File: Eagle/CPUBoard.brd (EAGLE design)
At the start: 100 x 80 mm, 33 parts, among them IC2 MAX232, IC3 MAX485CPA, J1 DISPLAY, J2 BUTTON_BOARD, J3 RELAY_BOARD, Q1 12.000MHz, X6 MKDSN1,5/3-5,08, X7 MKDSN1,5/3-5,08

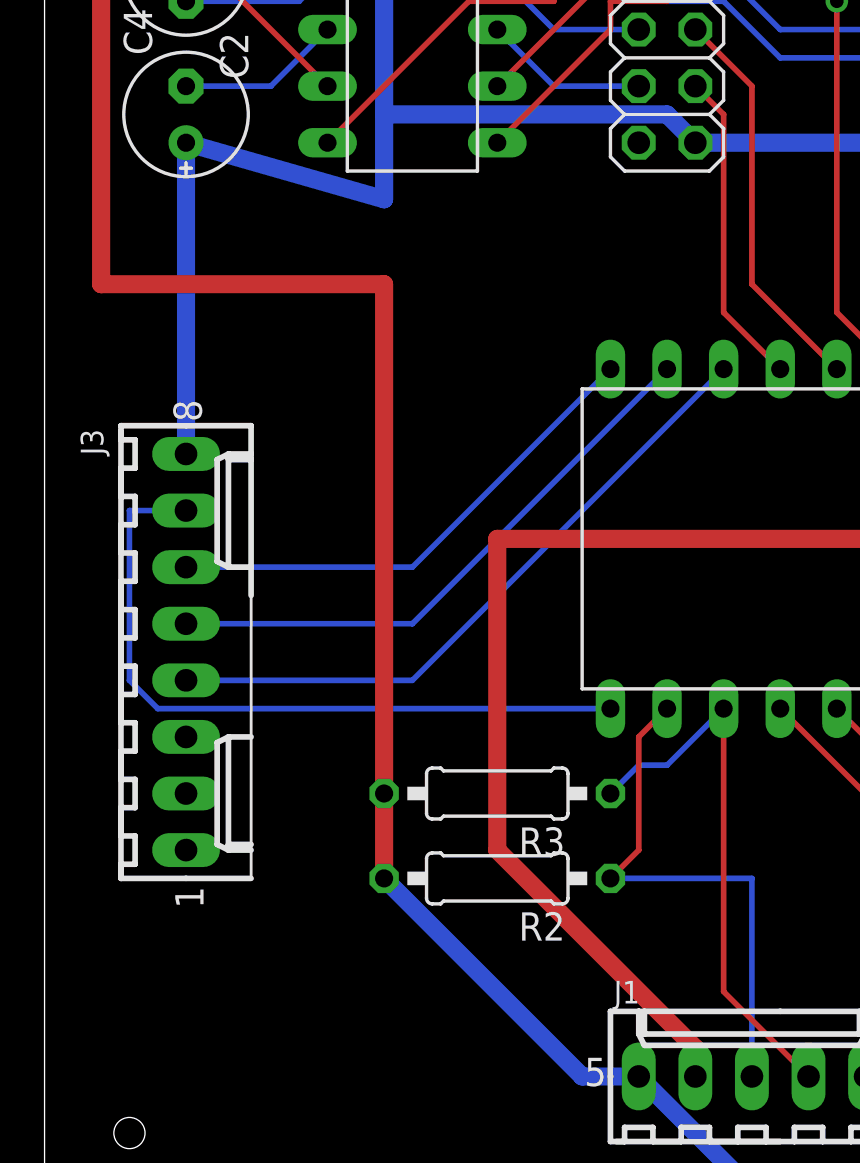
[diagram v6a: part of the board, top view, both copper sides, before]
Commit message: - swapped connections to relay board1
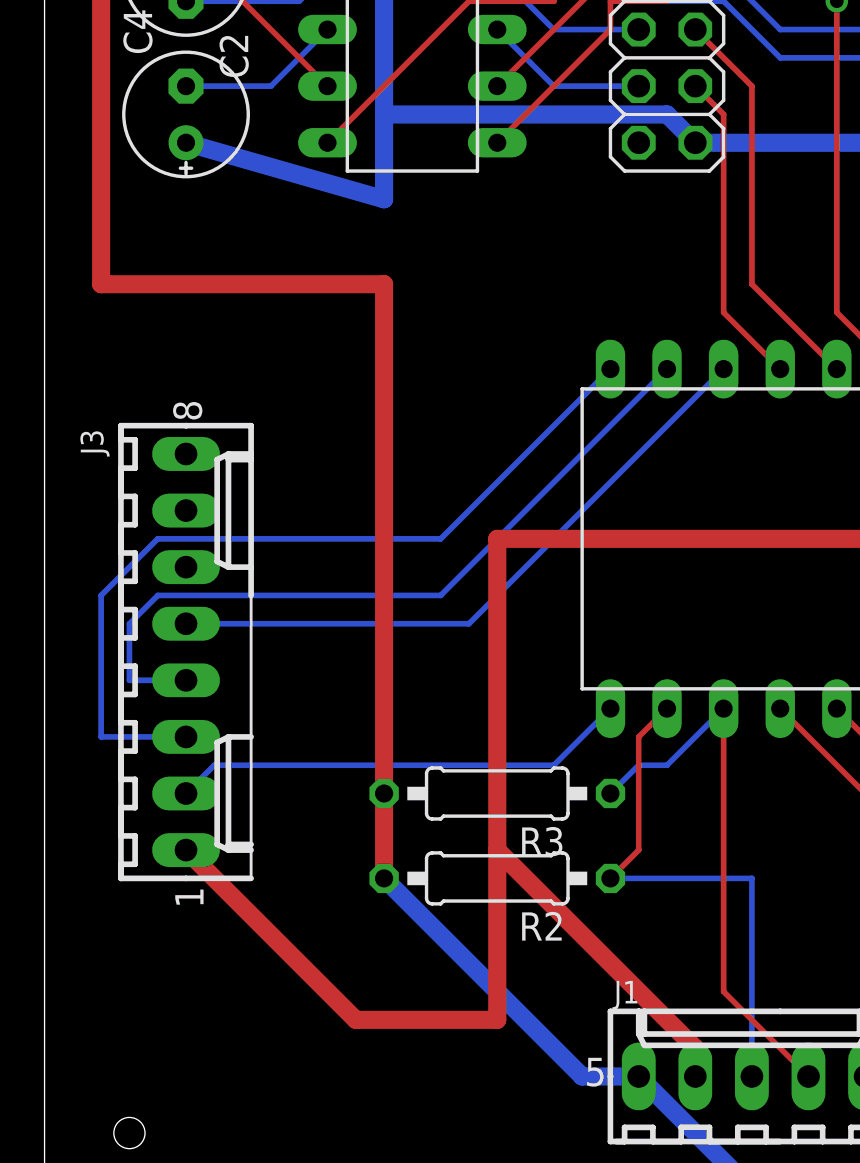
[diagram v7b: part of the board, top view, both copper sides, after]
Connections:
- net GND: now also J3.1; no longer J3.8
- net REL1: now also J3.2; no longer J3.7
- net REL2: now also J3.3; no longer J3.6
- net REL3: now also J3.4; no longer J3.5
- net REL4: now also J3.5; no longer J3.4
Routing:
- net REL2: track 22.7 -> 37.2 mm
- net REL1: track 32.3 -> 20.6 mm
- net GND: track 400.4 -> 411.2 mm
- net REL3: track 26.3 -> 33.9 mm
- net REL4: track 29.9 -> 28.9 mm
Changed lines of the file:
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@@
 <contactref element="J2" pad="10"/>
 <contactref element="JP1" pad="10"/>
-<contactref element="J3" pad="8"/>
-<wire x1="6.35" y1="34.29" x2="6.35" y2="48.26" width="0.8128" layer="16"/>
 <wire x1="45.72" y1="10.16" x2="49.53" y2="6.35" width="0.8128" layer="1"/>
 <wire x1="45.72" y1="17.78" x2="45.72" y2="10.16" width="0.8128" layer="1"/>
@@
 <wire x1="48.26" y1="44.45" x2="48.26" y2="38.1" width="0.8128" layer="16"/>
 <wire x1="43.18" y1="49.53" x2="48.26" y2="44.45" width="0.8128" layer="16"/>
+<contactref element="J3" pad="1"/>
+<wire x1="13.97" y1="8.89" x2="6.35" y2="16.51" width="0.8128" layer="1"/>
+<wire x1="20.32" y1="8.89" x2="13.97" y2="8.89" width="0.8128" layer="1"/>
+<wire x1="20.32" y1="16.51" x2="20.32" y2="8.89" width="0.8128" layer="1"/>
 </signal>
 <signal name="N$1">
@@
 <signal name="REL1">
 <contactref element="IC1" pad="21"/>
-<contactref element="J3" pad="7"/>
-<wire x1="5.08" y1="22.86" x2="25.4" y2="22.86" width="0.254" layer="16"/>
-<wire x1="3.81" y1="24.13" x2="5.08" y2="22.86" width="0.254" layer="16"/>
-<wire x1="3.81" y1="31.75" x2="3.81" y2="24.13" width="0.254" layer="16"/>
-<wire x1="6.35" y1="31.75" x2="3.81" y2="31.75" width="0.254" layer="16"/>
+<contactref element="J3" pad="2"/>
+<wire x1="22.86" y1="20.32" x2="25.4" y2="22.86" width="0.254" layer="16"/>
+<wire x1="7.62" y1="20.32" x2="22.86" y2="20.32" width="0.254" layer="16"/>
+<wire x1="6.35" y1="19.05" x2="7.62" y2="20.32" width="0.254" layer="16"/>
 </signal>
 <signal name="REL2">
 <contactref element="IC1" pad="20"/>
-<contactref element="J3" pad="6"/>
-<wire x1="16.51" y1="29.21" x2="25.4" y2="38.1" width="0.254" layer="16"/>
-<wire x1="6.35" y1="29.21" x2="16.51" y2="29.21" width="0.254" layer="16"/>
+<contactref element="J3" pad="3"/>
+<wire x1="17.78" y1="30.48" x2="25.4" y2="38.1" width="0.254" layer="16"/>
+<wire x1="5.08" y1="30.48" x2="17.78" y2="30.48" width="0.254" layer="16"/>
+<wire x1="2.54" y1="27.94" x2="5.08" y2="30.48" width="0.254" layer="16"/>
+<wire x1="2.54" y1="21.59" x2="2.54" y2="27.94" width="0.254" layer="16"/>
+<wire x1="6.35" y1="21.59" x2="2.54" y2="21.59" width="0.254" layer="16"/>
 </signal>
 <signal name="REL3">
 <contactref element="IC1" pad="19"/>
-<contactref element="J3" pad="5"/>
-<wire x1="16.51" y1="26.67" x2="27.94" y2="38.1" width="0.254" layer="16"/>
-<wire x1="6.35" y1="26.67" x2="16.51" y2="26.67" width="0.254" layer="16"/>
+<contactref element="J3" pad="4"/>
+<wire x1="17.78" y1="27.94" x2="27.94" y2="38.1" width="0.254" layer="16"/>
+<wire x1="5.08" y1="27.94" x2="17.78" y2="27.94" width="0.254" layer="16"/>
+<wire x1="3.81" y1="26.67" x2="5.08" y2="27.94" width="0.254" layer="16"/>
+<wire x1="3.81" y1="24.13" x2="3.81" y2="26.67" width="0.254" layer="16"/>
+<wire x1="6.35" y1="24.13" x2="3.81" y2="24.13" width="0.254" layer="16"/>
 </signal>
 <signal name="REL4">
 <contactref element="IC1" pad="18"/>
-<contactref element="J3" pad="4"/>
-<wire x1="16.51" y1="24.13" x2="30.48" y2="38.1" width="0.254" layer="16"/>
-<wire x1="6.35" y1="24.13" x2="16.51" y2="24.13" width="0.254" layer="16"/>
+<contactref element="J3" pad="5"/>
+<wire x1="19.05" y1="26.67" x2="30.48" y2="38.1" width="0.254" layer="16"/>
+<wire x1="6.35" y1="26.67" x2="19.05" y2="26.67" width="0.254" layer="16"/>
 </signal>
 <signal name="SER1_RTS">

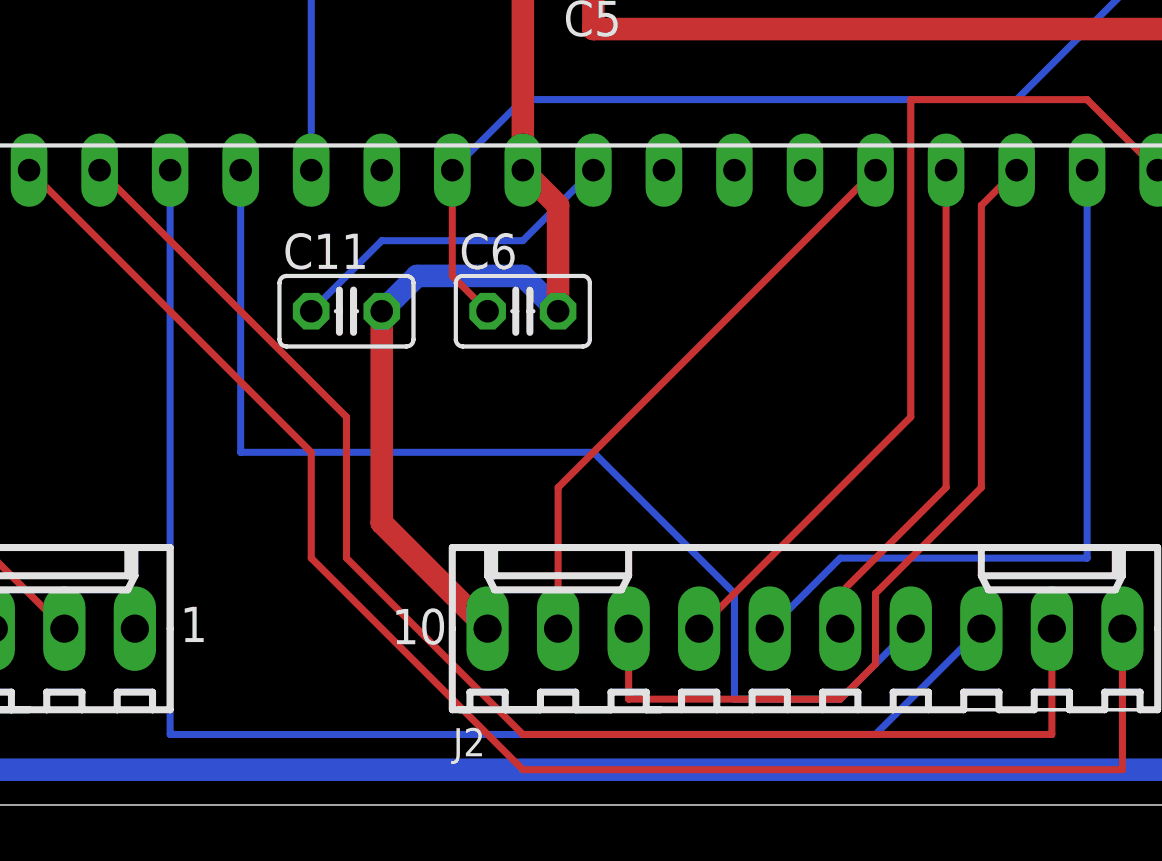
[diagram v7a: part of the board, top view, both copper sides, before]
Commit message: - swapped LED_L and LED_R in schematic - solder bridge between two buttons found and fixed
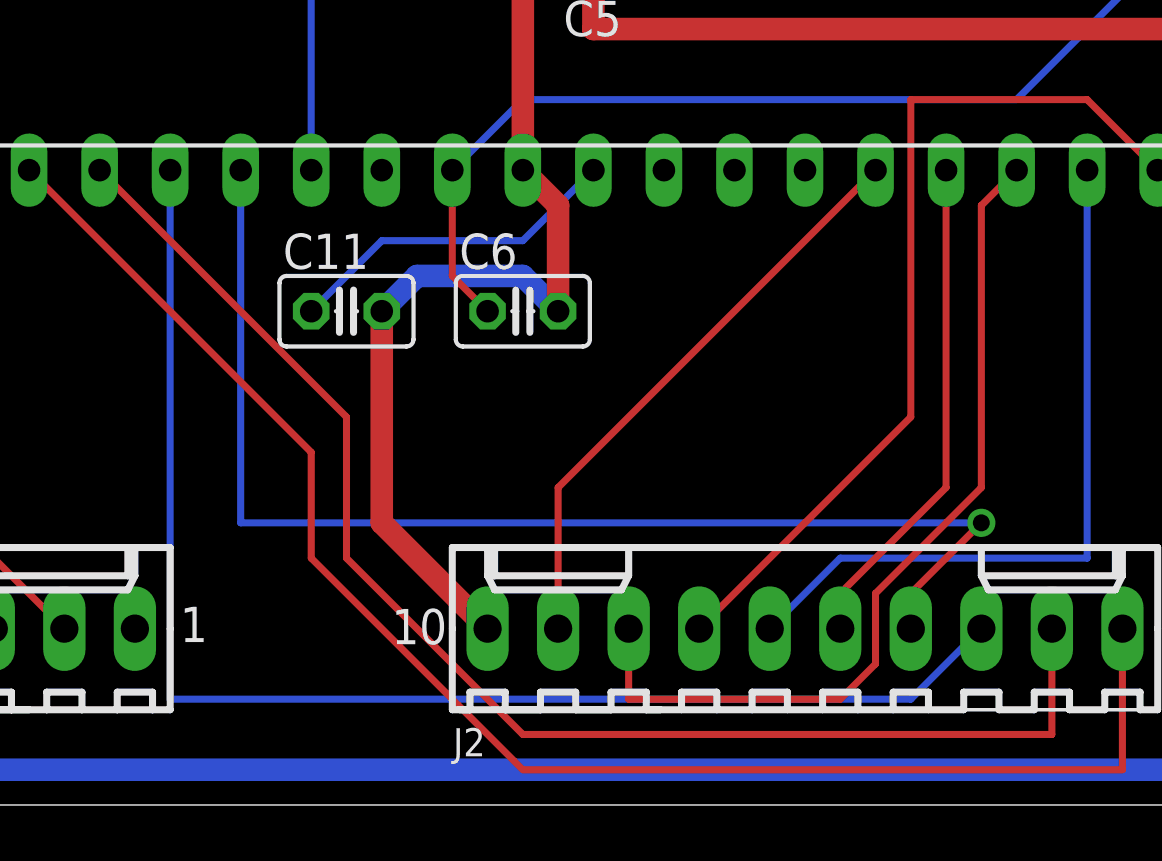
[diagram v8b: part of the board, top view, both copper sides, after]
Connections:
- net LED_L: now also IC1.27, J2.4; no longer IC1.26, J2.3
- net LED_R: now also IC1.26, J2.3; no longer IC1.27, J2.4
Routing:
- net LED_R: track 41.3 -> 49.3 mm
- net LED_L: track 51.1 -> 44.2 mm, vias 0 -> 1
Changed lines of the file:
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@@
 </signal>
 <signal name="LED_L">
+<contactref element="IC1" pad="27"/>
+<contactref element="J2" pad="4"/>
+<wire x1="40.64" y1="10.16" x2="40.64" y2="22.86" width="0.254" layer="16"/>
+<wire x1="67.31" y1="10.16" x2="40.64" y2="10.16" width="0.254" layer="16"/>
+<wire x1="64.77" y1="7.62" x2="67.31" y2="10.16" width="0.254" layer="1"/>
+<wire x1="64.77" y1="6.35" x2="64.77" y2="7.62" width="0.254" layer="1"/>
+<via x="67.31" y="10.16" extent="1-16" drill="0.6096"/>
+</signal>
+<signal name="LED_R">
 <contactref element="IC1" pad="26"/>
 <contactref element="J2" pad="3"/>
-<wire x1="38.1" y1="2.54" x2="38.1" y2="22.86" width="0.254" layer="16"/>
-<wire x1="63.5" y1="2.54" x2="38.1" y2="2.54" width="0.254" layer="16"/>
-<wire x1="67.31" y1="6.35" x2="63.5" y2="2.54" width="0.254" layer="16"/>
-</signal>
-<signal name="LED_R">
-<contactref element="IC1" pad="27"/>
-<contactref element="J2" pad="4"/>
-<wire x1="40.64" y1="12.7" x2="40.64" y2="22.86" width="0.254" layer="16"/>
-<wire x1="53.34" y1="12.7" x2="40.64" y2="12.7" width="0.254" layer="16"/>
-<wire x1="58.42" y1="7.62" x2="53.34" y2="12.7" width="0.254" layer="16"/>
-<wire x1="58.42" y1="3.81" x2="58.42" y2="7.62" width="0.254" layer="16"/>
-<wire x1="62.23" y1="3.81" x2="58.42" y2="3.81" width="0.254" layer="16"/>
-<wire x1="64.77" y1="6.35" x2="62.23" y2="3.81" width="0.254" layer="16"/>
+<wire x1="38.1" y1="3.81" x2="38.1" y2="22.86" width="0.254" layer="16"/>
+<wire x1="64.77" y1="3.81" x2="38.1" y2="3.81" width="0.254" layer="16"/>
+<wire x1="67.31" y1="6.35" x2="64.77" y2="3.81" width="0.254" layer="16"/>
 </signal>
 <signal name="PRESET_LEFT">
